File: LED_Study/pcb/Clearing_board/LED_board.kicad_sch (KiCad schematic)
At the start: 4 parts

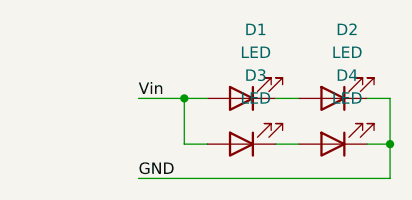
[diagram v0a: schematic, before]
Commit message: updated boards and ordered from PCBway
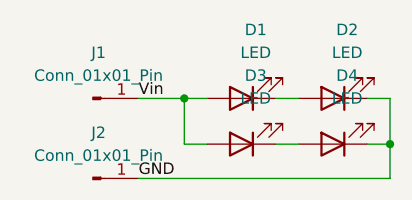
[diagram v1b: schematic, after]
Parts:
- added J1, J2: Conn_01x01_Pin, Connector_PinHeader_1.00mm:PinHeader_1x01_P1.00mm_Vertical, symbol Connector:Conn_01x01_Pin
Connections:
- net GND: now also J2.1 (Pin_1)
- net Vin: now also J1.1 (Pin_1)
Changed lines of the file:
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@@
+    )
+  )
+  (symbol (lib_id "Connector:Conn_01x01_Pin") (at 68.58 48.26 0) (unit 1)
+    (in_bom yes) (on_board yes) (dnp no) (fields_autoplaced)
+    (property "Reference" "J2" (at 69.215 43.18 0)
+      (effects (font (size 1.27 1.27)))
+    )
+    (property "Value" "Conn_01x01_Pin" (at 69.215 45.72 0)
+      (effects (font (size 1.27 1.27)))
+    )
+    (property "Footprint" "Connector_PinHeader_1.00mm:PinHeader_1x01_P1.00mm_Vertical" (at 68.58 48.26 0)
+      (effects (font (size 1.27 1.27)) hide)
+    )
+    (property "Datasheet" "~" (at 68.58 48.26 0)
+      (effects (font (size 1.27 1.27)) hide)
+    )
+    (pin "1")
+    (instances
+      (project "LED_board"
+        (path "/ee3210f4-4163-4542-8403-a0d7023a83cd"
+          (reference "J2") (unit 1)
+        )
+      )
+    )
+  )
+  (symbol (lib_id "Connector:Conn_01x01_Pin") (at 68.58 39.37 0) (unit 1)
+    (in_bom yes) (on_board yes) (dnp no) (fields_autoplaced)
+    (property "Reference" "J1" (at 69.215 34.29 0)
+      (effects (font (size 1.27 1.27)))
+    )
+    (property "Value" "Conn_01x01_Pin" (at 69.215 36.83 0)
+      (effects (font (size 1.27 1.27)))
+    )
+    (property "Footprint" "Connector_PinHeader_1.00mm:PinHeader_1x01_P1.00mm_Vertical" (at 68.58 39.37 0)
+      (effects (font (size 1.27 1.27)) hide)
+    )
+    (property "Datasheet" "~" (at 68.58 39.37 0)
+      (effects (font (size 1.27 1.27)) hide)
+    )
+    (pin "1")
+    (instances
+      (project "LED_board"
+        (path "/ee3210f4-4163-4542-8403-a0d7023a83cd"
+          (reference "J1") (unit 1)
+        )
+      )
     )
   )
